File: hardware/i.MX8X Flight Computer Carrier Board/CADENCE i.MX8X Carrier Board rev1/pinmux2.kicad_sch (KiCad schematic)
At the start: 0 parts

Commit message: reorged pin definitions page
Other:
- note added: "Reference Page"
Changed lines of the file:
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@@
 	(generator_version "9.0")
 	(paper "A4")
+	(text "Reference\nPage"
+		(exclude_from_sim no)
+		(at 258.064 25.908 0)
+		(effects
+			(font
+				(size 6.35 6.35)
+				(thickness 1.27)
+				(bold yes)
+			)
+		)
+	)
 	(image
 		(at 96.52 99.822)

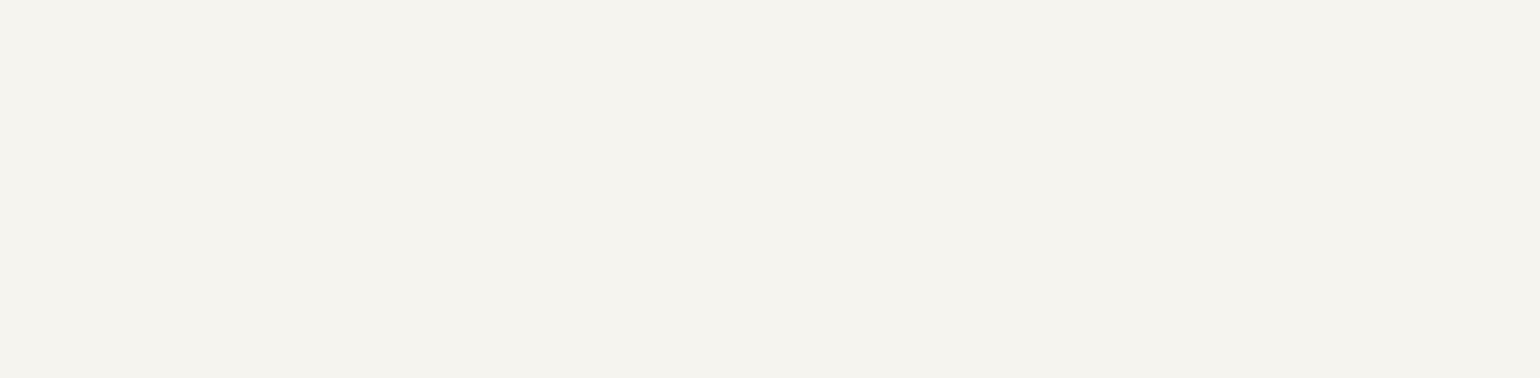
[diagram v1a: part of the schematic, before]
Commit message: Some ERC fixes, schematic annotations, pinmux for uSD & GPIO fixes, GPIO level shifter, footprint selection & pathway fix
component footprints for most part have been selected
going to double check again tmr
imx8x som bth samtec connector footprint needs to be adjusted as reference footprint uses each connector as individual symbol, while we have as part of one symbol (spacing between connector is important so som can fit in)
also one component didnt have part (uart mux) and havent assigned
implemented can bus interface with satnogs, moved around gpios, level shifted 8 gpios, fixed few missing connections (gps 1pps, a load switch enable gpio), resolved some erc errors/ symbol shorts, incorrect pinmux implementation around A9&10 for uSD and gpio, reannotated schematic, fixed footprint reference paths
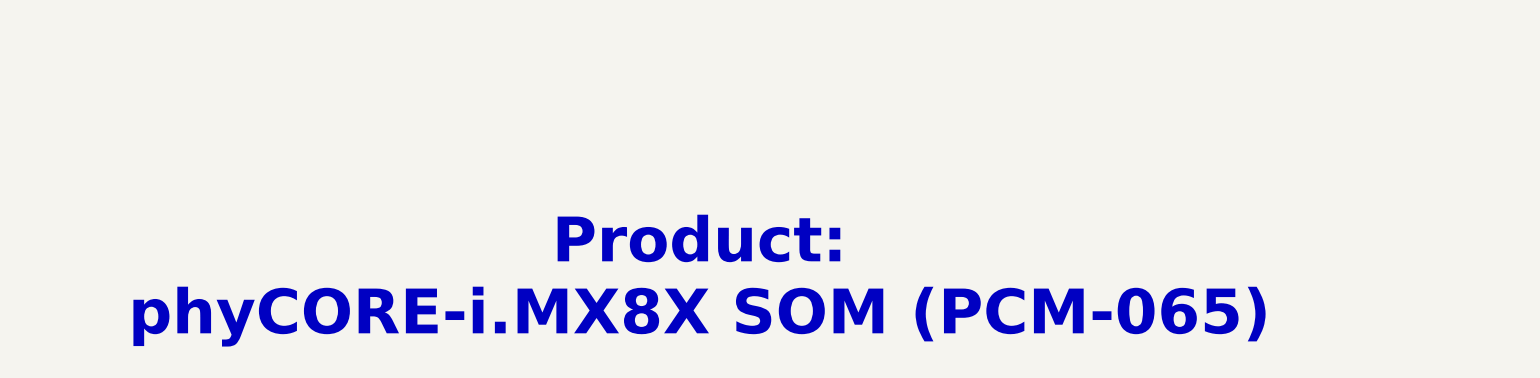
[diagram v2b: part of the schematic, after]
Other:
- note added: "Product: phyCORE-i.MX8X SOM (PCM-065)"
